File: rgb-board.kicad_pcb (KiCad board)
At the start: 2 copper layers, 178 x 129.5 mm, 84 parts, among them J1 Conn_02x25_Odd_Even, J2 SCART-F, J5 DE15_Plug_HighDensity_Mountin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, J6 SJ1-3535NG, K1 G6K-2PY-12DC, Q101 BC850C, Q105 BC850C, Q109 BC850C, Q113 BC850C, Q114 BC850C, Q201 BC850C, SW1 SW_DPDT_x2, SW2 SPUJ193700, U1 NCP1117-12_SOT223

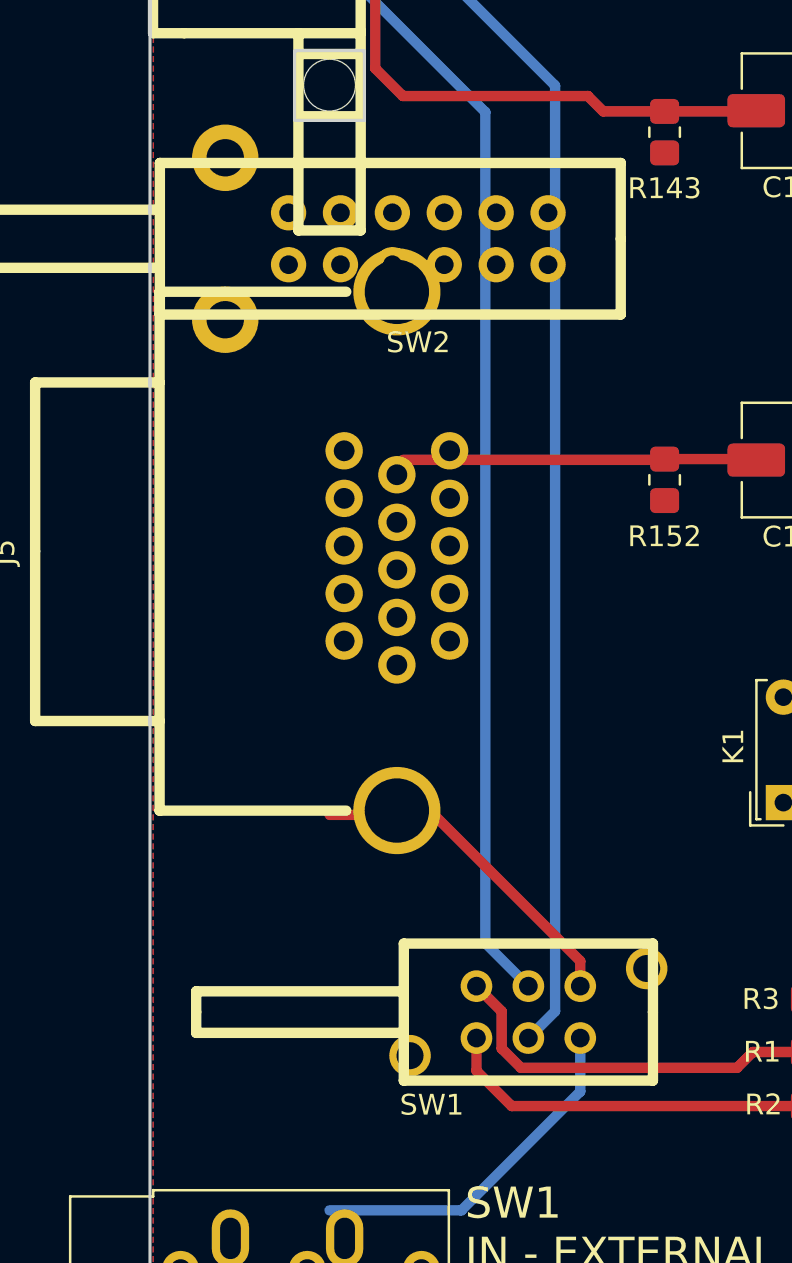
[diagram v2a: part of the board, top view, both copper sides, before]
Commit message: Add ALPS SPUJ Series push switches footprints library. Replace LC2259 and PBH4UEE push switches with ALPS SPUJ190900 and SPUJ193700. Remove LC2259 and PBH4UEE footprints.
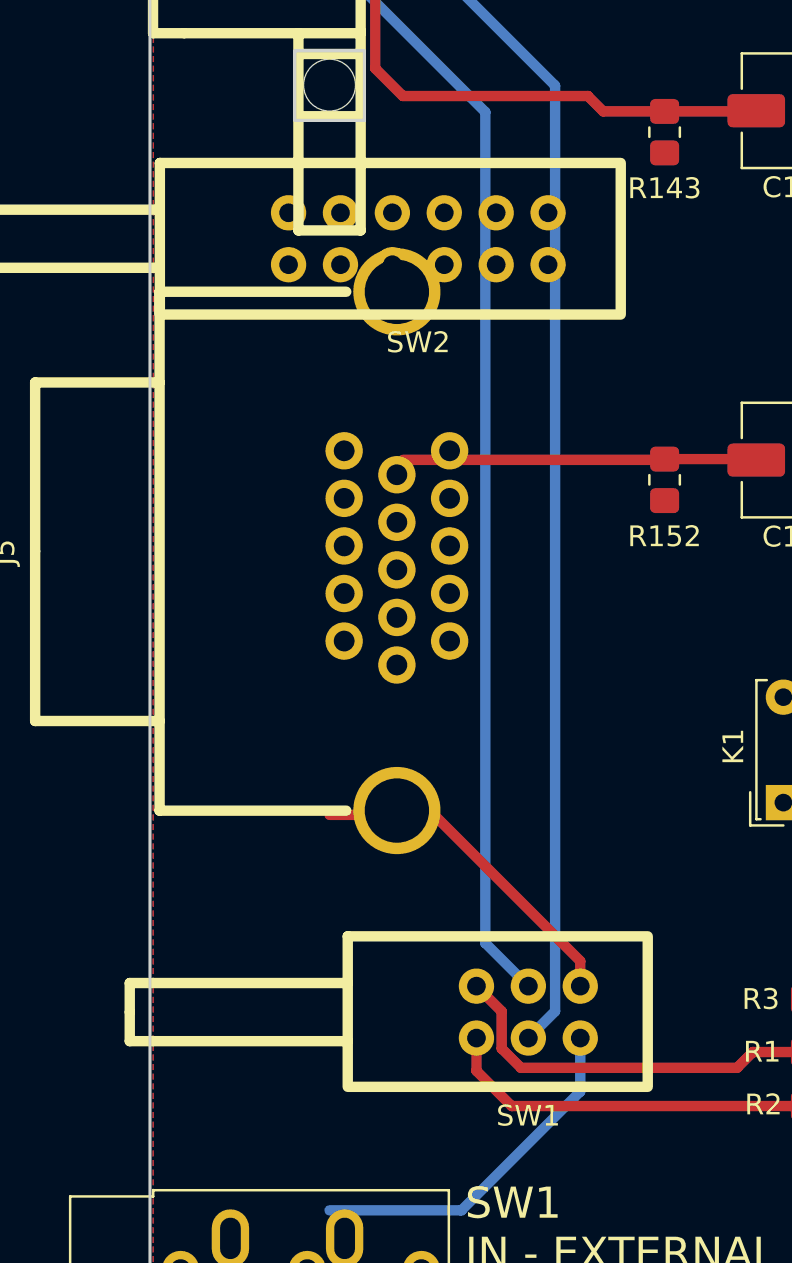
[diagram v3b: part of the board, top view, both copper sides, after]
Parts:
- SW1: footprint LC2259:LC2259 -> ALPS_SPUJ:SPUJ190900
- SW2: footprint PBH4UEE:PBH4UEE -> ALPS_SPUJ:SPUJ193700
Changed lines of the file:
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@@
 		)
 	)
-	(footprint "LC2259:LC2259"
+	(footprint "ALPS_SPUJ:SPUJ190900"
 		(layer "F.Cu")
 		(at 68.05 140)
 		(property "Reference" "SW1"
-			(at -4.65 4.475 0)
+			(at 0 5 0)
 			(layer "F.SilkS")
 			(effects
@@
 		)
 		(property "Value" "SW_DPDT_x2"
-			(at 0 -4.3 0)
+			(at 0 -5 0)
 			(layer "F.Fab")
 			(effects
@@
 			)
 		)
-		(property "Footprint" "LC2259:LC2259"
-			(at 0 0 0)
+		(property "Footprint" "ALPS_SPUJ:SPUJ190900"
+			(at 3.75 0 0)
 			(unlocked yes)
 			(layer "F.Fab")
@@
 		)
 		(property "Datasheet" ""
-			(at 0 0 0)
+			(at 3.75 0 0)
 			(unlocked yes)
 			(layer "F.Fab")
@@
 		)
 		(property "Description" ""
-			(at 0 0 0)
+			(at 3.75 0 0)
 			(unlocked yes)
 			(layer "F.Fab")
@@
 		(attr through_hole)
 		(fp_line
-			(start -16 -1)
-			(end -6 -1)
+			(start -19.2 -1.4)
+			(end -8.7 -1.4)
 			(stroke
 				(width 0.5)
@@
 		)
 		(fp_line
-			(start -16 0)
-			(end -16 -1)
+			(start -19.2 0)
+			(end -19.2 -1.4)
 			(stroke
 				(width 0.5)
@@
 		)
 		(fp_line
-			(start -16 0)
-			(end -16 1)
+			(start -19.2 0)
+			(end -19.2 1.4)
 			(stroke
 				(width 0.5)
@@
 		)
 		(fp_line
-			(start -16 1)
-			(end -6 1)
+			(start -19.2 1.4)
+			(end -8.7 1.4)
 			(stroke
 				(width 0.5)
@@
 			(layer "F.SilkS")
 		)
-		(fp_line
-			(start -6 -3.3)
-			(end -6 3.3)
+		(fp_rect
+			(start -8.7 -3.65)
+			(end 5.75 3.6)
 			(stroke
 				(width 0.5)
-				(type solid)
-			)
-			(layer "F.SilkS")
-		)
-		(fp_line
-			(start -6 3.3)
-			(end 6 3.3)
-			(stroke
-				(width 0.5)
-				(type solid)
-			)
-			(layer "F.SilkS")
-		)
-		(fp_line
-			(start 6 -3.3)
-			(end -6 -3.3)
-			(stroke
-				(width 0.5)
-				(type solid)
-			)
-			(layer "F.SilkS")
-		)
-		(fp_line
-			(start 6 0)
-			(end 6 -3.3)
-			(stroke
-				(width 0.5)
-				(type solid)
-			)
-			(layer "F.SilkS")
-		)
-		(fp_line
-			(start 6 3.3)
-			(end 6 0)
-			(stroke
-				(width 0.5)
-				(type solid)
+				(type default)
 			)
+			(fill none)
 			(layer "F.SilkS")
 		)
 		(pad "1" thru_hole circle
-			(at -2.5 -1.25)
-			(size 1.524 1.524)
+			(at 2.5 1.25)
+			(size 1.7 1.7)
 			(drill 0.9)
 			(layers "*.Cu" "*.Mask")
@@
 		)
 		(pad "2" thru_hole circle
-			(at 0 -1.25)
-			(size 1.524 1.524)
+			(at 0 1.25)
+			(size 1.7 1.7)
 			(drill 0.9)
 			(layers "*.Cu" "*.Mask")
@@
 		)
 		(pad "3" thru_hole circle
-			(at 2.5 -1.25)
-			(size 1.524 1.524)
+			(at -2.5 1.25)
+			(size 1.7 1.7)
 			(drill 0.9)
 			(layers "*.Cu" "*.Mask")
@@
 		)
 		(pad "4" thru_hole circle
-			(at -2.5 1.25)
-			(size 1.524 1.524)
+			(at 2.5 -1.25)
+			(size 1.7 1.7)
 			(drill 0.9)
 			(layers "*.Cu" "*.Mask")
@@
 		)
 		(pad "5" thru_hole circle
-			(at 0 1.25)
-			(size 1.524 1.524)
+			(at 0 -1.25)
+			(size 1.7 1.7)
 			(drill 0.9)
 			(layers "*.Cu" "*.Mask")
@@
 		)
 		(pad "6" thru_hole circle
-			(at 2.5 1.25)
-			(size 1.524 1.524)
+			(at -2.5 -1.25)
+			(size 1.7 1.7)
 			(drill 0.9)
 			(layers "*.Cu" "*.Mask")
@@
 			(pintype "passive")
 		)
-		(pad "S" thru_hole circle
-			(at -5.7 2.1)
-			(size 2 2)
-			(drill 1.3)
-			(layers "*.Cu" "*.Mask")
-			(remove_unused_layers no)
-		)
-		(pad "S" thru_hole circle
-			(at 5.7 -2.1)
-			(size 2 2)
-			(drill 1.3)
-			(layers "*.Cu" "*.Mask")
-			(remove_unused_layers no)
-		)
 	)
 	(footprint "Package_TO_SOT_SMD:SOT-23_Handsoldering"
@@
 		)
 	)
-	(footprint "PBH4UEE:PBH4UEE"
+	(footprint "ALPS_SPUJ:SPUJ193700"
 		(layer "F.Cu")
 		(at 62.75 102.75)
@@
 			)
 		)
-		(property "Footprint" "PBH4UEE:PBH4UEE"
+		(property "Footprint" "ALPS_SPUJ:SPUJ193700"
 			(at 0 0 0)
 			(unlocked yes)
@@
 			(layer "F.SilkS")
 		)
-		(fp_line
+		(fp_rect
 			(start -12.45 -3.65)
-			(end -12.45 3.65)
-			(stroke
-				(width 0.5)
-				(type solid)
-			)
-			(layer "F.SilkS")
-		)
-		(fp_line
-			(start -12.45 -3.65)
-			(end 9.75 -3.65)
-			(stroke
-				(width 0.5)
-				(type solid)
-			)
-			(layer "F.SilkS")
-		)
-		(fp_line
-			(start -12.45 3.65)
 			(end 9.75 3.65)
 			(stroke
 				(width 0.5)
-				(type solid)
-			)
-			(layer "F.SilkS")
-		)
-		(fp_line
-			(start 9.75 -3.65)
-			(end 9.75 0)
-			(stroke
-				(width 0.5)
-				(type solid)
-			)
-			(layer "F.SilkS")
-		)
-		(fp_line
-			(start 9.75 3.65)
-			(end 9.75 0)
-			(stroke
-				(width 0.5)
-				(type solid)
+				(type default)
 			)
+			(fill none)
 			(layer "F.SilkS")
 		)
@@
 			(pintype "bidirectional")
 		)
-		(pad "S" thru_hole circle
-			(at -9.3 -3.9)
-			(size 3.2 3.2)
-			(drill 1.8)
-			(layers "*.Cu" "*.Mask")
-			(remove_unused_layers no)
-		)
-		(pad "S" thru_hole circle
-			(at -9.3 3.9)
-			(size 3.2 3.2)
-			(drill 1.8)
-			(layers "*.Cu" "*.Mask")
-			(remove_unused_layers no)
-		)
 	)
